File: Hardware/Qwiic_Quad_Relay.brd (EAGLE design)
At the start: 82.5 x 47 mm, 119 parts, among them J2 Qwiic Right Angle, J3 Qwiic Right Angle, J4 AVR_SPI_PROG_3X2TESTPOINTS, J9 POWER_JACK, K1 RELAY-SPDT-JZC-11F, K2 RELAY-SPDT-JZC-11F, K3 RELAY-SPDT-JZC-11F, K4 RELAY-SPDT-JZC-11F, Q1 600mA/40V, Q2 600mA/40V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

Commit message: Example Code, Firmware, Changes to board
Example Code is not done, firmware as well, unless I want to add a bit more to toggle all channels to opposite states. Production Files have been added. Induction resistor has been changed to a 100 Ohm resistor.
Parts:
- R1, R12, R13, R14: value 10 -> 100
- R8: value 10K -> 10k
- U1: value V_REG_317SMD -> (none)
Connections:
- net 5V: now also U1.4
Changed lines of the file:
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@@
 <layer number="19" name="Unrouted" color="6" fill="1" visible="yes" active="yes"/>
 <layer number="20" name="Dimension" color="15" fill="1" visible="yes" active="yes"/>
-<layer number="21" name="tPlace" color="16" fill="1" visible="no" active="yes"/>
+<layer number="21" name="tPlace" color="16" fill="1" visible="yes" active="yes"/>
 <layer number="22" name="bPlace" color="14" fill="1" visible="yes" active="yes"/>
 <layer number="23" name="tOrigins" color="15" fill="1" visible="yes" active="yes"/>
@@
 <layer number="44" name="Drills" color="7" fill="1" visible="no" active="yes"/>
 <layer number="45" name="Holes" color="7" fill="1" visible="yes" active="yes"/>
-<layer number="46" name="Milling" color="3" fill="1" visible="yes" active="yes"/>
+<layer number="46" name="Milling" color="3" fill="1" visible="no" active="yes"/>
 <layer number="47" name="Measures" color="7" fill="1" visible="no" active="yes"/>
 <layer number="48" name="Document" color="7" fill="1" visible="no" active="yes"/>
@@
 <wire x1="69.85" y1="19.05" x2="68.707" y2="19.05" width="0.1524" layer="46"/>
 <wire x1="65.913" y1="19.05" x2="64.77" y2="19.05" width="0.1524" layer="46"/>
-<text x="69.342" y="19.812" size="0.381" layer="20" font="vector" rot="R90">Route Out</text>
+<text x="69.342" y="19.812" size="0.381" layer="46" font="vector" rot="R90">Route Out</text>
 <dimension x1="24.13" y1="21.59" x2="25.273" y2="21.59" x3="24.7015" y3="18.161" textsize="0.508" textratio="15" layer="47" dtype="horizontal" unit="inch"/>
 <dimension x1="44.45" y1="21.463" x2="45.593" y2="21.463" x3="45.0215" y3="18.161" textsize="0.508" textratio="15" layer="47" dtype="horizontal" unit="inch"/>
@@
 <attribute name="SF_SKU" value="COM-00100" x="10.16" y="19.05" size="1.778" layer="27" rot="R90" display="off"/>
 </element>
-<element name="R1" library="SparkFun-Resistors" package="0603" value="10" x="4.953" y="28.194">
-<attribute name="PROD_ID" value="RES-07871" x="4.953" y="28.194" size="1.778" layer="27" display="off"/>
+<element name="R1" library="SparkFun-Resistors" package="0603" value="100" x="4.953" y="28.194">
+<attribute name="PROD_ID" value="RES-07863" x="4.953" y="28.194" size="1.778" layer="27" display="off"/>
 </element>
 <element name="R4" library="SparkFun-Resistors" package="0603" value="220" x="19.05" y="26.67">
@@
 <element name="JP6" library="SparkFun-Aesthetics" package="FIDUCIAL-1X2" value="FIDUCIAL1X2" x="5.08" y="2.54" rot="MR0"/>
 <element name="J4" library="SparkFun-Connectors" package="2X3_TEST_POINTS" value="AVR_SPI_PROG_3X2TESTPOINTS" x="31.115" y="37.973" rot="MR180"/>
-<element name="R8" library="SparkFun-Resistors" package="0603" value="10K" x="37.592" y="38.227" rot="R90">
-<attribute name="PROD_ID" value="RES-00818" x="37.592" y="38.227" size="1.778" layer="27" font="vector" ratio="15" rot="R90" display="off"/>
+<element name="R8" library="SparkFun-Resistors" package="0603" value="10k" x="37.592" y="38.227" rot="R90">
+<attribute name="PROD_ID" value="RES-00824" x="37.592" y="38.227" size="1.778" layer="27" font="vector" ratio="15" rot="R90" display="off"/>
 </element>
 <element name="R9" library="SparkFun-Resistors" package="0603" value="1k" x="60.198" y="42.164">
-<attribute name="PROD_ID" value="RES-00818" x="60.198" y="42.164" size="1.778" layer="27" font="vector" ratio="15" display="off"/>
+<attribute name="PROD_ID" value="RES-07856" x="60.198" y="42.164" size="1.778" layer="27" font="vector" ratio="15" display="off"/>
 </element>
 <element name="D3" library="SparkFun-LED" package="LED-0603" value="RED" x="60.071" y="44.069">
@@
 <attribute name="PROD_ID" value="DIO-11623" x="24.13" y="26.67" size="1.778" layer="27" font="vector" ratio="15" display="off"/>
 </element>
-<element name="R12" library="SparkFun-Resistors" package="0603" value="10" x="24.13" y="28.194">
-<attribute name="PROD_ID" value="RES-07871" x="24.13" y="28.194" size="1.778" layer="27" font="vector" ratio="15" display="off"/>
-</element>
-<element name="R13" library="SparkFun-Resistors" package="0603" value="10" x="44.45" y="28.194">
-<attribute name="PROD_ID" value="RES-07871" x="44.45" y="28.194" size="1.778" layer="27" font="vector" ratio="15" display="off"/>
-</element>
-<element name="R14" library="SparkFun-Resistors" package="0603" value="10" x="64.77" y="28.321">
-<attribute name="PROD_ID" value="RES-07871" x="64.77" y="28.321" size="1.778" layer="27" font="vector" ratio="15" display="off"/>
+<element name="R12" library="SparkFun-Resistors" package="0603" value="100" x="24.13" y="28.194">
+<attribute name="PROD_ID" value="RES-07863" x="24.13" y="28.194" size="1.778" layer="27" font="vector" ratio="15" display="off"/>
+</element>
+<element name="R13" library="SparkFun-Resistors" package="0603" value="100" x="44.45" y="28.194">
+<attribute name="PROD_ID" value="RES-07863" x="44.45" y="28.194" size="1.778" layer="27" font="vector" ratio="15" display="off"/>
+</element>
+<element name="R14" library="SparkFun-Resistors" package="0603" value="100" x="64.77" y="28.321">
+<attribute name="PROD_ID" value="RES-07863" x="64.77" y="28.321" size="1.778" layer="27" font="vector" ratio="15" display="off"/>
 </element>
 <element name="D7" library="SparkFun-LED" package="LED-0603" value="BLUE" x="35.814" y="29.21" rot="R270">
@@
 <attribute name="PROD_ID" value="CONN-08197" x="70.612" y="50.038" size="1.778" layer="27" rot="R180" display="off"/>
 </element>
-<element name="U1" library="SparkFun-IC-Power" package="SOT223" value="V_REG_317SMD" x="52.705" y="40.513"/>
+<element name="U1" library="SparkFun-IC-Power" package="SOT223" value="" x="52.705" y="40.513">
+<attribute name="PROD_ID" value="VREG-08170" x="52.705" y="40.513" size="1.778" layer="27" display="off"/>
+</element>
 <element name="R6" library="SparkFun-Resistors" package="0603" value="240" x="51.816" y="35.052">
 <attribute name="PROD_ID" value="RES-07849" x="51.816" y="35.052" size="1.778" layer="27" display="off"/>
@@
 <via x="53.4035" y="39.9415" extent="1-16" drill="0.508"/>
 <wire x1="5.803" y1="28.194" x2="5.803" y2="31.203" width="0.254" layer="1"/>
+<contactref element="U1" pad="4"/>
 </signal>
 <signal name="N$19">

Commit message: Updates to board file, example code, and firmware for release!
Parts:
- R1, R12, R13, R14: value 100 -> 10
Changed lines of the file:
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@@
 <attribute name="SF_SKU" value="COM-00100" x="10.16" y="19.05" size="1.778" layer="27" rot="R90" display="off"/>
 </element>
-<element name="R1" library="SparkFun-Resistors" package="0603" value="100" x="4.953" y="28.194">
-<attribute name="PROD_ID" value="RES-07863" x="4.953" y="28.194" size="1.778" layer="27" display="off"/>
+<element name="R1" library="SparkFun-Resistors" package="0603" value="10" x="4.953" y="28.194">
+<attribute name="PROD_ID" value="RES-09834" x="4.953" y="28.194" size="1.778" layer="27" display="off"/>
 </element>
 <element name="R4" library="SparkFun-Resistors" package="0603" value="220" x="19.05" y="26.67">
@@
 <attribute name="PROD_ID" value="DIO-11623" x="24.13" y="26.67" size="1.778" layer="27" font="vector" ratio="15" display="off"/>
 </element>
-<element name="R12" library="SparkFun-Resistors" package="0603" value="100" x="24.13" y="28.194">
-<attribute name="PROD_ID" value="RES-07863" x="24.13" y="28.194" size="1.778" layer="27" font="vector" ratio="15" display="off"/>
+<element name="R12" library="SparkFun-Resistors" package="0603" value="10" x="24.13" y="28.194">
+<attribute name="PROD_ID" value="RES-09834" x="24.13" y="28.194" size="1.778" layer="27" font="vector" ratio="15" display="off"/>
 </element>
-<element name="R13" library="SparkFun-Resistors" package="0603" value="100" x="44.45" y="28.194">
-<attribute name="PROD_ID" value="RES-07863" x="44.45" y="28.194" size="1.778" layer="27" font="vector" ratio="15" display="off"/>
+<element name="R13" library="SparkFun-Resistors" package="0603" value="10" x="44.45" y="28.194">
+<attribute name="PROD_ID" value="RES-09834" x="44.45" y="28.194" size="1.778" layer="27" font="vector" ratio="15" display="off"/>
 </element>
-<element name="R14" library="SparkFun-Resistors" package="0603" value="100" x="64.77" y="28.321">
-<attribute name="PROD_ID" value="RES-07863" x="64.77" y="28.321" size="1.778" layer="27" font="vector" ratio="15" display="off"/>
+<element name="R14" library="SparkFun-Resistors" package="0603" value="10" x="64.77" y="28.321">
+<attribute name="PROD_ID" value="RES-09834" x="64.77" y="28.321" size="1.778" layer="27" font="vector" ratio="15" display="off"/>
 </element>
 <element name="D7" library="SparkFun-LED" package="LED-0603" value="BLUE" x="35.814" y="29.21" rot="R270">

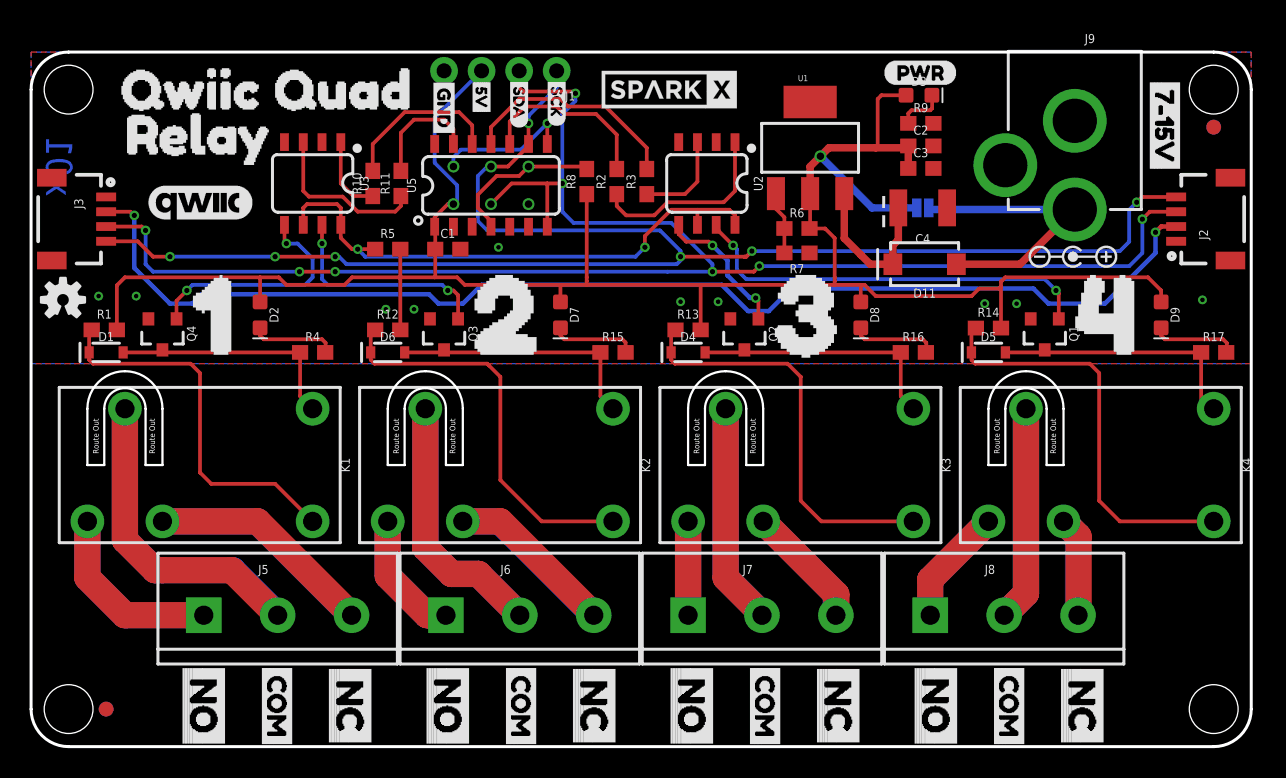
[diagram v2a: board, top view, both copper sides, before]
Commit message: Version x02
Changes:
Added thermal polygon around and underneath the voltage regulator.
Changed LED resistor values to 1k because they were too bright.
Added address jumper.
Modified relay pins
Changed Firmware to add second I2C address
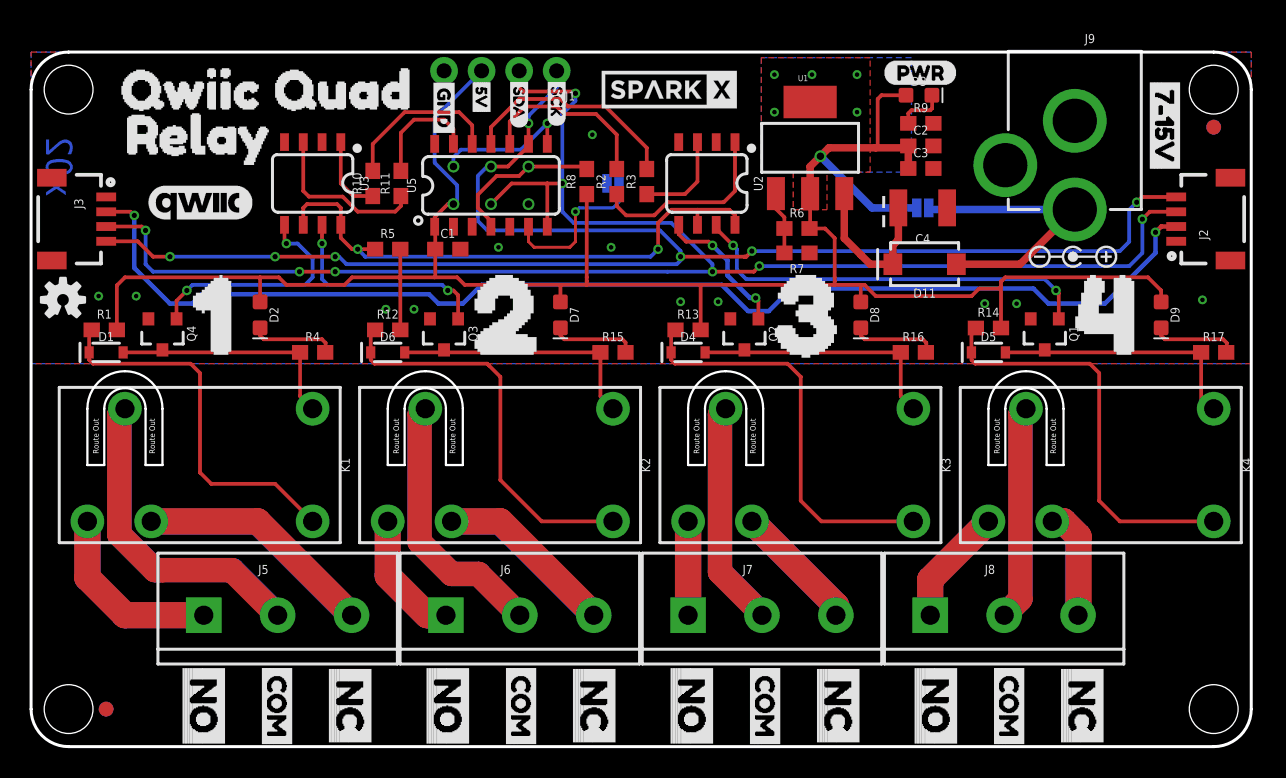
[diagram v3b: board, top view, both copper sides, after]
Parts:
- added JP10: JUMPER-SMT_2_NO_SILK, SparkFun-Jumpers:SMT-JUMPER_2_NO_SILK
- added U$56: (no value), Labels:ADR-()-04
- R15, R16, R17, R4: value 220 -> 1k
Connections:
- new net ADDR_JUMP: JP10.1, U5.6
- net GND: now also JP10.2
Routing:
- net ADDR_JUMP: track 0.00 -> 11.0 mm, vias 0 -> 1
- net NC4: track 13.5 -> 15.1 mm
- net NC2: track 23.0 -> 24.5 mm
- net NC1: track 30.8 -> 32.4 mm
- net COM3: track 30.0 -> 30.6 mm
- net COM2: track 35.4 -> 36.0 mm
- net COM1: track 42.7 -> 43.3 mm
- net NC3: track 16.8 -> 17.4 mm
- net N$6: track 37.9 -> 38.5 mm
- net 5V: vias 1 -> 6
- added copper zone on layer 1, net 5V
- added copper zone on layer 16, net 5V
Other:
- board text added: "x02"
- board text removed: "x01"
